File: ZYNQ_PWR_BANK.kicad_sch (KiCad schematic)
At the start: 1 part, among them U1 XC7Z020-2CLG484I

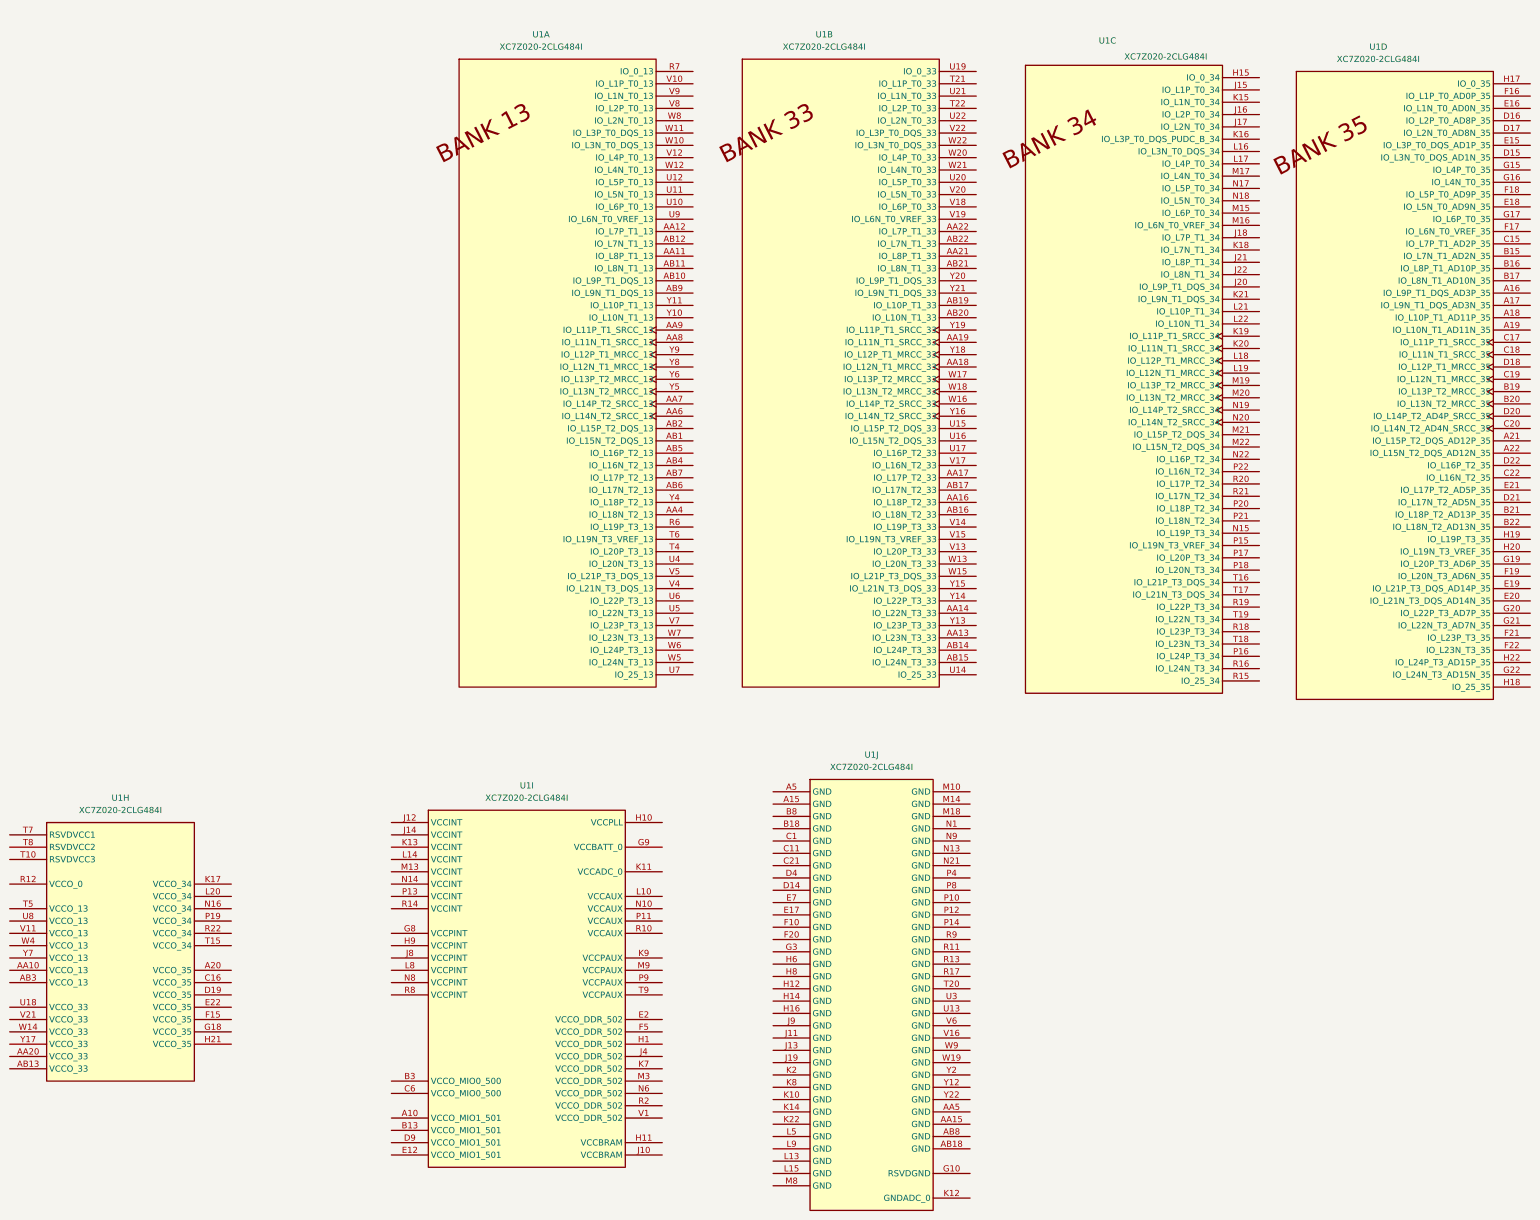
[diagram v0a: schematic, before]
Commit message: Refactor schematic hierarchy and add PL Ethernet
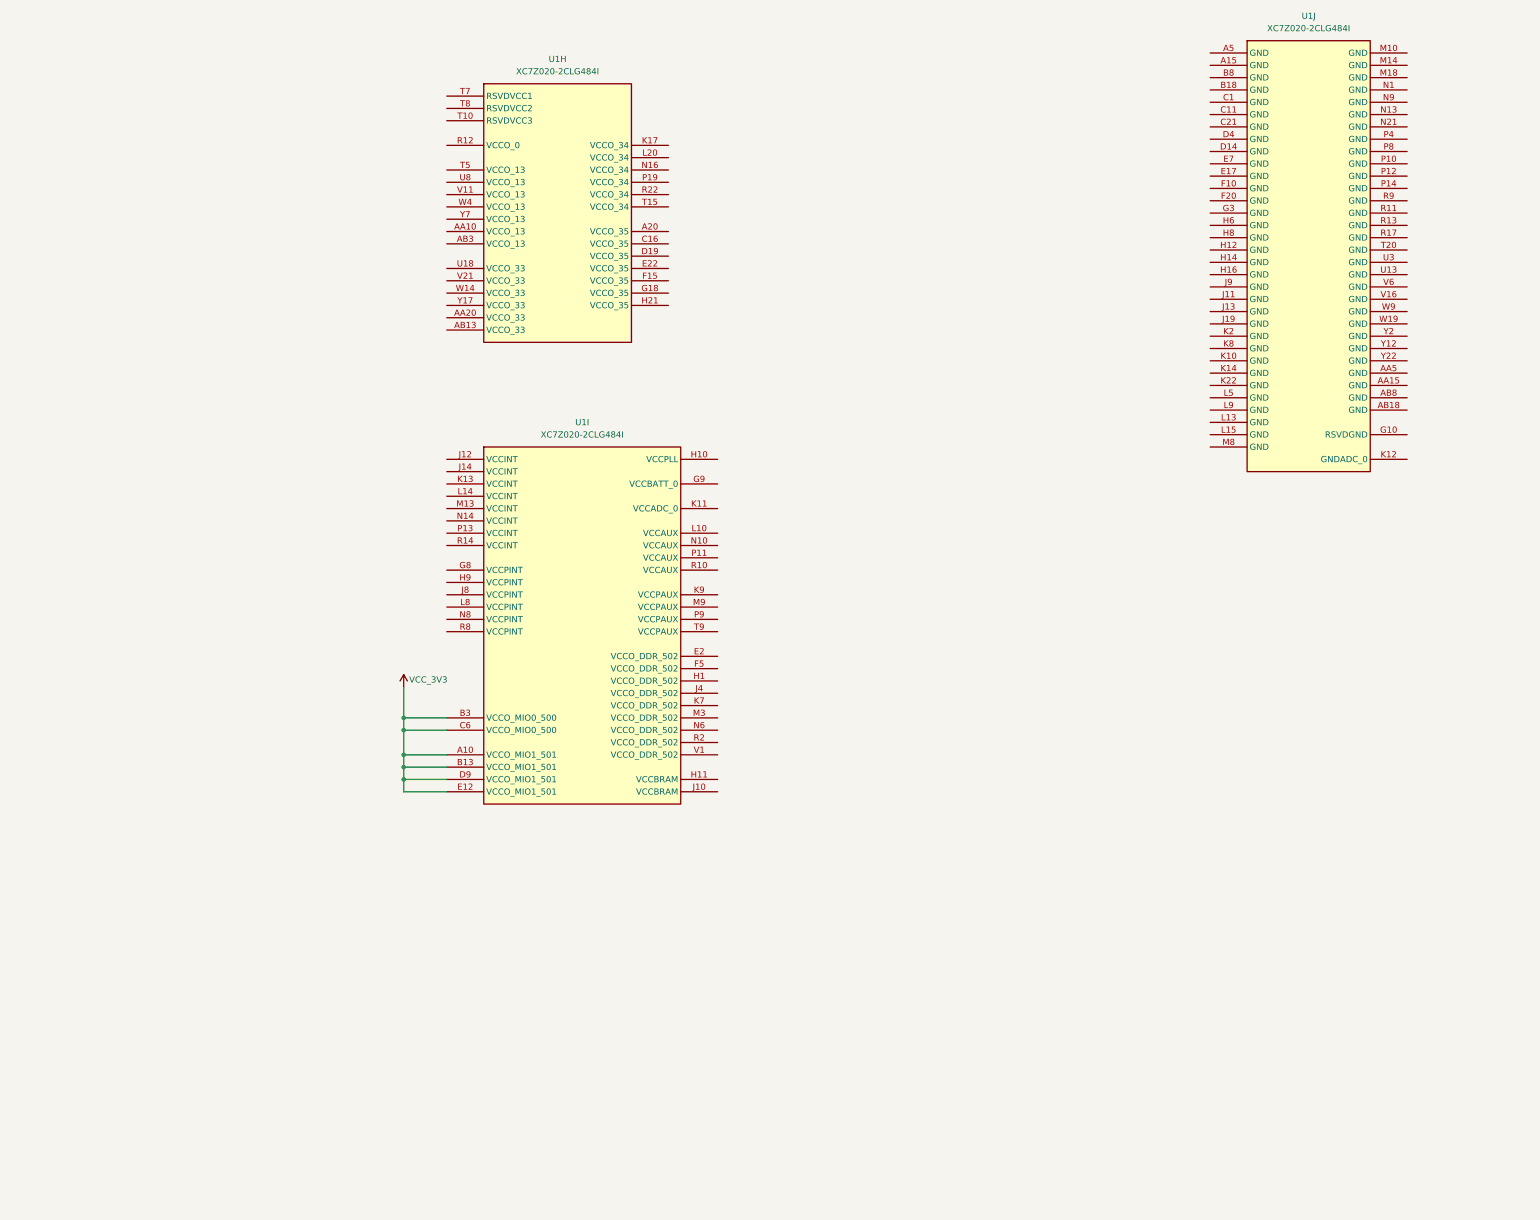
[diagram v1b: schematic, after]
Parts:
- removed unit 2 of U1
- removed unit 1 of U1
- removed unit 4 of U1
- removed unit 3 of U1
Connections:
- net VCC_3V3: now reaches U1.A10 (VCCO_MIO1_501)
- net VCC_3V3: now also U1.B13 (VCCO_MIO1_501), U1.B3 (VCCO_MIO0_500), U1.C6 (VCCO_MIO0_500), U1.D9 (VCCO_MIO1_501), U1.E12 (VCCO_MIO1_501)
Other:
- moved on the sheet: U1H, U1I, U1J
